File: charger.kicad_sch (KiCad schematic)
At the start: 19 parts, among them U1 IP2326

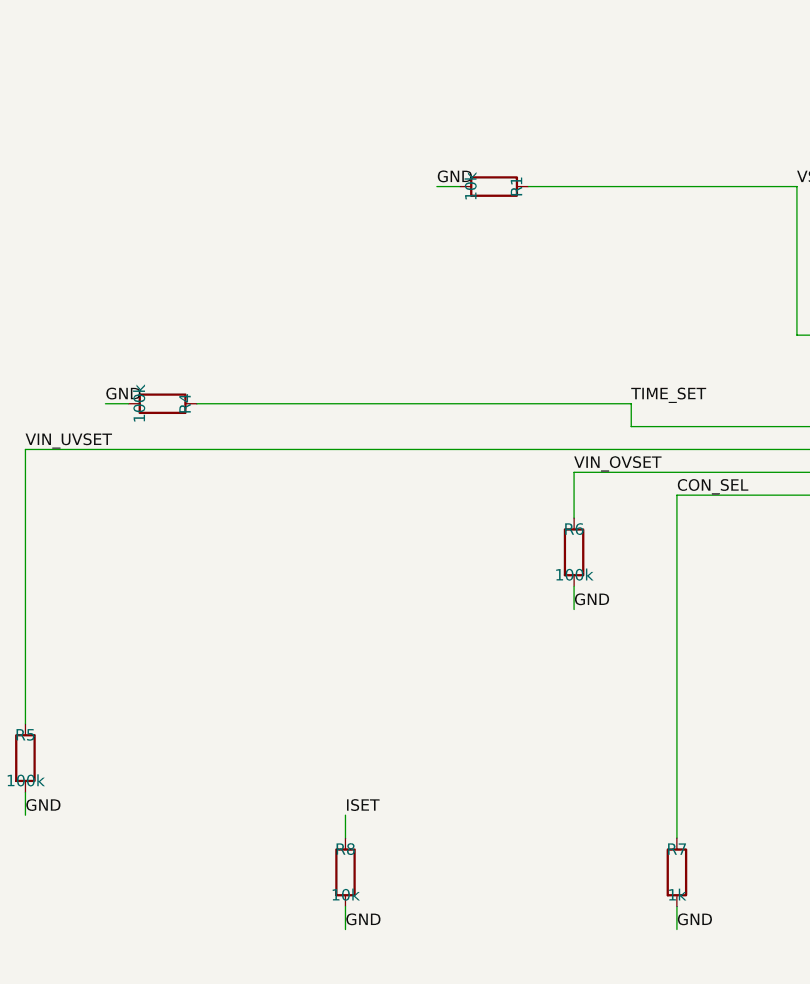
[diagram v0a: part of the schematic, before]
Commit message: components: lock buckboost FETs, R5 SLOPE, and charger config-R values
Buckboost Q1-Q4:
- AON7544 (LCSC C315567), 30V/30A, 5mOhm@10V, DFN-8 3x3, 183k stock,
  ~$0.12 @ qty 1-49.  Extended tier — per feedback_assembly_tier_cost
  memory, that's fine (the cost cliff is Standard-assembly tier, not
  Extended library type).  At 5A steady x 5mOhm = 25mW per FET
  conduction loss, well under the 23W package limit.
- Symbol + footprint + 3D model imported via easyeda2kicad for C315567,
  same workflow as IP2326.

Buckboost R5 (SLOPE):
- Was 10k placeholder.  Set to 20k per LM5176 §9.3.7 slope-compensation
  calc.  Inductor downslope Sn = (Vin_max=12.6V / L=6.8uH) x
  Rcs=5mOhm = ~9.3 mV/us; required Se >= Sn/2 = 4.6 mV/us to avoid
  sub-harmonic oscillation.  20k is TI-EVM starting point at this
  Fsw/L combo; safe against sub-harmonic and leaves loop-tune headroom.
  Notes property records bench-verification guidance.

Charger config-R updates:
- R1 (VSET) 10k → 100k — IP2326 §10 default for 12.6V float on 3S.
- R8 (ISET) 10k → 33k — I_chg ≈ 66/R_iset (kOhm) → 33k = 2A charge,
  0.67C for a 3Ah 3S pack.  Was 10k which would have set an
  unsafe ~6.6A charge rate.
- R2, R3, R4, R5, R6, R9, R10, R7 already at IP2326-typical values
  (verified via table in commit thread); no change needed.

Full-project ERC: 0 errors, 33 cosmetic warnings.  The 2 leftover
"SOIC-8 footprint not found" warnings from the placeholder Device:
Q_NMOS symbols are gone.

Co-Authored-By: Claude Opus 4.7 <noreply@anthropic.com>
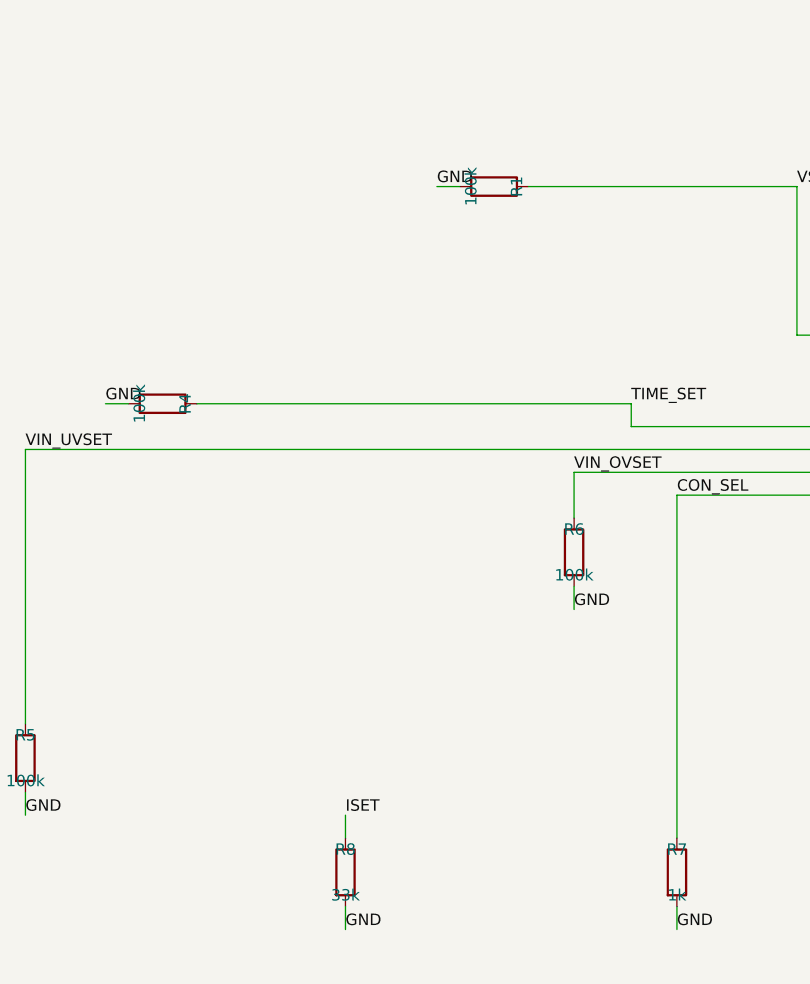
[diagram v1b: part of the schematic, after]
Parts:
- R1: value 10k -> 100k; Notes (none) -> IP2326 VSET default, sets 12.6V float for 3S per datasheet 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
- R8: value 10k -> 33k; Notes (none) -> IP2326 ISET: I_chg ≈ 66 / R_iset (kOhm). 33k → 2A charge = 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

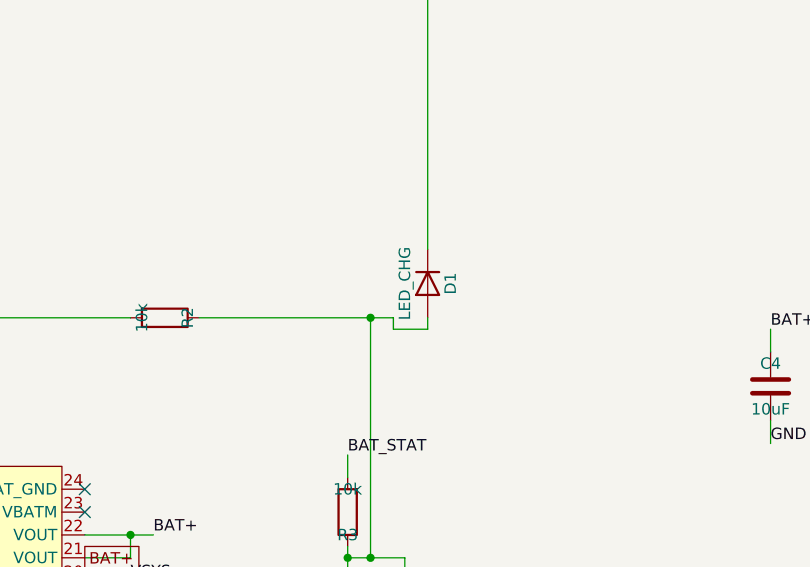
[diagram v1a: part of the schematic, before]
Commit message: sourcing: lock LCSC + MPN + Manufacturer + Footprint for every remaining BOM line
Applied JLCPCB picks (LCSC number + manufacturer part number + tuned
footprint) across all four sub-sheets — 72 components total.  Every
placed component now carries LCSC, MPN, and Manufacturer properties;
the built-in Value/Footprint fields point to the exact JLCPCB stock
unit for that pick.

Highlights:
- ICs (Preferred where available, Extended otherwise):
    U1(bms)      BQ7692003PWR   C601650    TSSOP-20
    U1(charger)  IP2326         C2832094   VQFN-24 EP4x4
    U1(input)    CH224K         C970725    ESSOP-10
    U1(bckbst)   LM5176PWPR     C442493    HTSSOP-28
- Diodes + TVS (all Preferred tier):
    D1(input)    SRV05-4        C7420376   SOT-23-6   (622K stock)
    D2(input)    SMAJ12A        C19077531  SMA        ( 33K stock)
    D1-3(bms)    SMAJ15A        C19077535  SMA        (174K stock)
- Power passives:
    L1(bckbst)   6.8uH 5A       C167221    FXL0630-6R8-M  7x6.6mm
    L1(charger)  2.2uH 4.8A     C602029    FHD4020S-2R2MT 4x4mm
    FB1(input)   600R@100MHz    C139183    CBW160808U601T 0603 (1A)
    R9(bms)      5mR 2W ±1%     C185817    RLM25FEER005   2512
- Bulk passives — Uniohm 0603WAF series, ±1%, high stock.  All caps
  Samsung/Yageo 0603 or 0805 ceramic.  Reused Q1-Q4 = AON7544
  (already locked at 9120877) for bms.Q1/Q2 too — same part
  covers 30V/20A pack-return FET stack.

Effect on pre-fab readiness (kicad-happy):
- SS-001 error CLEARED — 1/34 MPN coverage was blocking pre-fab;
  now 34/34 (100%).
- DS-002 warning shifted: was "no datasheets" (2/34 MPNs), now
  "no datasheets dir" (34/34 MPNs).  Non-blocking; datasheet PDFs
  are nice-to-have but the review can proceed without them.
- 1 remaining error PP-001 (LM5176_VCC no DC source) is a false
  positive: KiCad library symbol declares VCC as power_in but it's
  actually the LM5176's internal 5V LDO OUTPUT.  Accepted as-is.

Full-project ERC still 0 errors.  Schematic is now sourcing-clean
and ready for 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
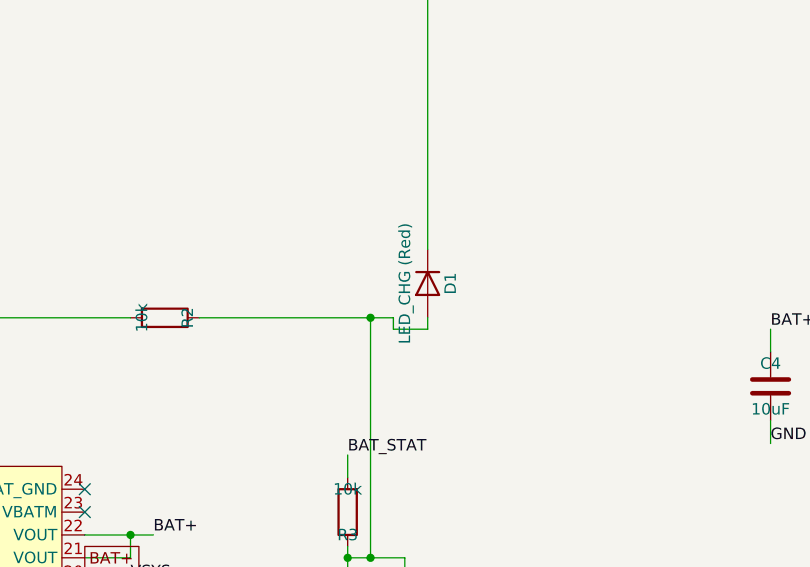
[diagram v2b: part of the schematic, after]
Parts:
- C1, C4: LCSC (none) -> C15850; MPN (none) -> CL21A106KAYNNNE; Manufacturer (none) -> SAMSUNG
- C2, C3: LCSC (none) -> C45783; MPN (none) -> CL21A226MAQNNNE; Manufacturer (none) -> SAMSUNG
- C5: LCSC (none) -> C14663; MPN (none) -> CC0603KRX7R9BB104; Manufacturer (none) -> YAGEO
- D1: value LED_CHG -> LED_CHG (Red); footprint (none) -> LED_SMD:LED_0603_1608Metric; LCSC (none) -> C2286; MPN (none) -> KT-0603R; Manufacturer (none) -> HUBEI KENTO ELEC
- L1: footprint (none) -> Inductor_SMD:L_Sunlord_MWSA0402S; LCSC (none) -> C602029; MPN (none) -> FHD4020S-2R2MT; Manufacturer (none) -> FH (Guangdong Fenghua)
- R1, R4, R5, R6, R9: LCSC (none) -> C25803; MPN (none) -> 0603WAF1003T5E; Manufacturer (none) -> Uniohm
- R10: LCSC (none) -> C23162; MPN (none) -> 0603WAF4701T5E; Manufacturer (none) -> Uniohm
- R2, R3: LCSC (none) -> C25804; MPN (none) -> 0603WAF1002T5E; Manufacturer (none) -> Uniohm
- R7: LCSC (none) -> C21190; MPN (none) -> 0603WAF1001T5E; Manufacturer (none) -> Uniohm
- R8: LCSC (none) -> C4216; MPN (none) -> 0603WAF3302T5E; Manufacturer (none) -> Uniohm
- TH1: footprint (none) -> Resistor_SMD:R_0603_1608Metric; LCSC (none) -> C2889048; MPN (none) -> CMFA 103F3435; Manufacturer (none) -> CHIP-TEK
- U1: footprint (none) -> power_module_lib:VQFN-24_L4.0-W4.0-P0.50-BL-EP2.5; LCSC (none) -> C2832094; MPN (none) -> IP2326; Manufacturer (none) -> INJOINIC

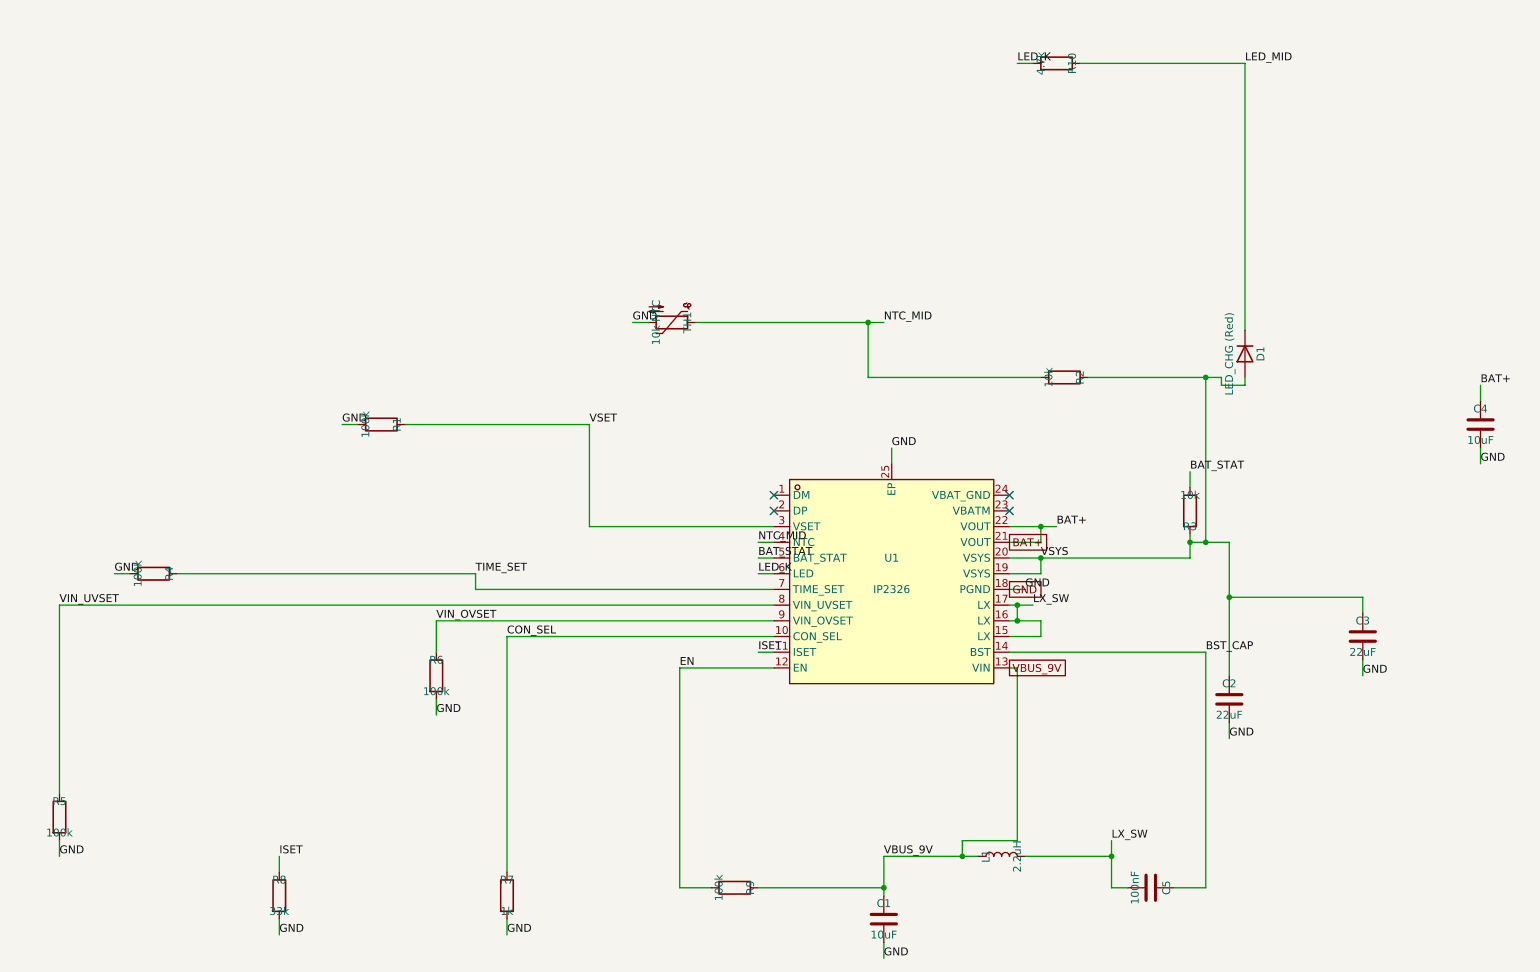
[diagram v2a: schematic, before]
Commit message: sheets: hierarchical ref disambiguation via annotate_schematic
Every sub-sheet symbol now carries a `_{SHEETNAME}{instance_num}` suffix so
refs are globally unique across the hierarchy.  76 refs rewritten:
  bms:       27 (e.g. U1 → U1_BMS1,      Q1 → Q1_BMS1)
  charger:   19 (e.g. U1 → U1_CHARGER1,  R7 → R7_CHARGER1)
  input:      8 (e.g. U1 → U1_INPUT1,    J1 → J1_INPUT1)
  buckboost: 22 (e.g. U1 → U1_BUCKBOOST1,Q1 → Q1_BUCKBOOST1)

Fixes kicad-cli's `schematic has annotation errors` warning which previously
caused BOM export to collapse the four different U1's (BQ76920 + IP2326 +
CH224K + LM5176) into a single row with comma-joined values.

bom_step1.csv committed alongside as the post-disambiguation baseline —
38 grouped rows, 100% LCSC/MPN coverage.

Applied via the new `annotate_schematic` hierarchical pass shipped in
KiCAD-MCP-Server c529efa on develop.  See NOTES.md for the mid-session
handoff block and memory `feedback_hierarchical_annotate`.

Co-Authored-By: Claude Opus 4.7 <noreply@anthropic.com>
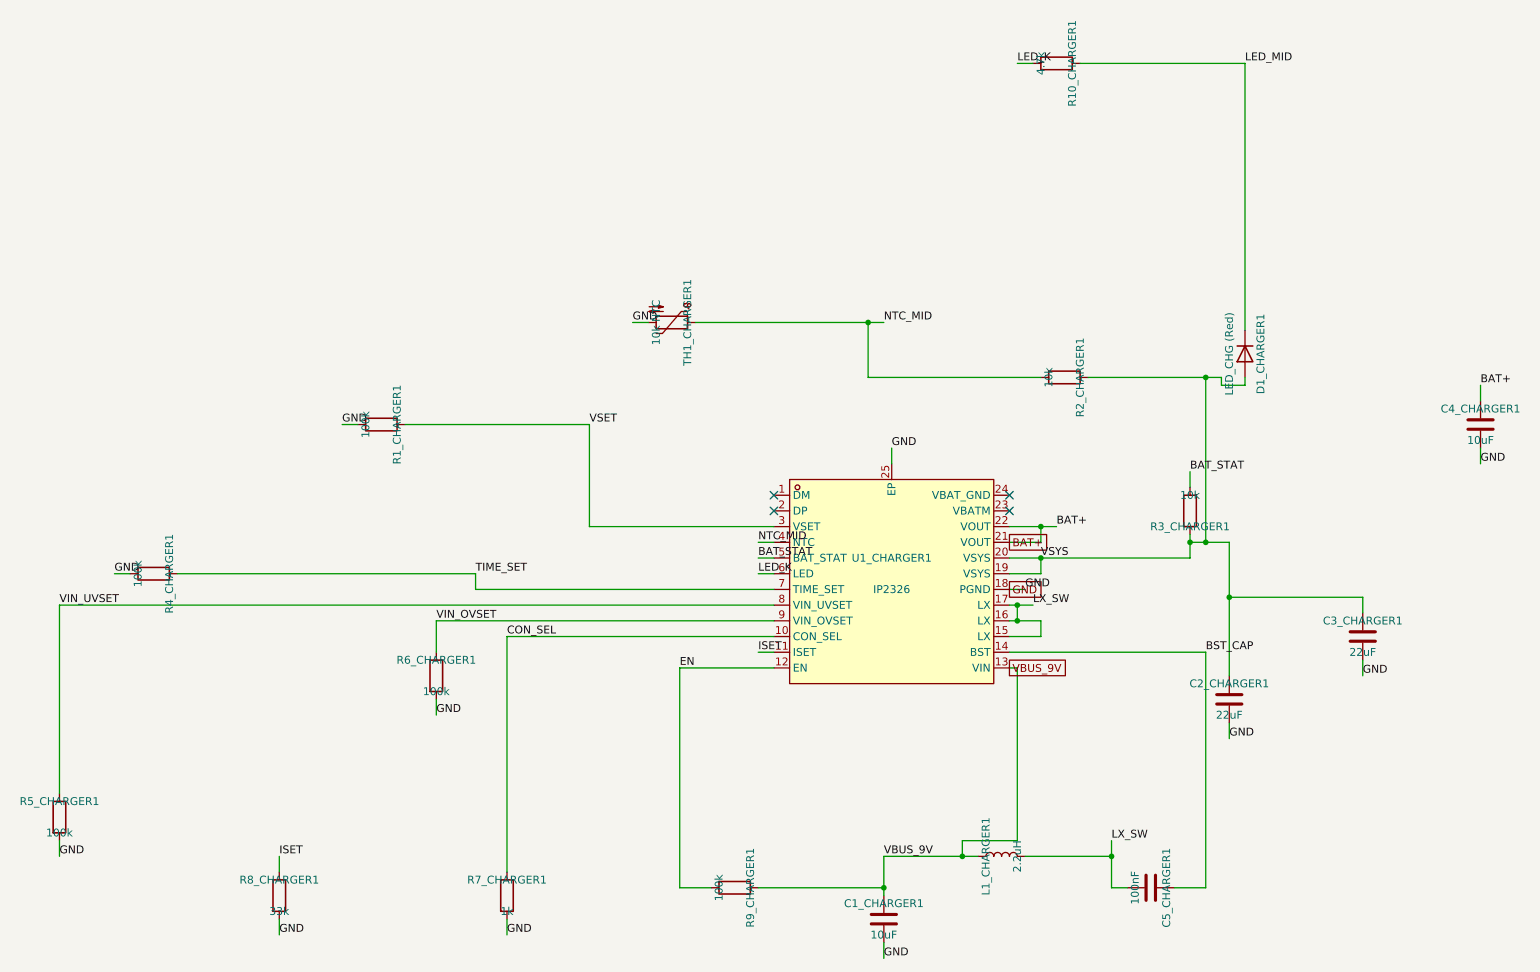
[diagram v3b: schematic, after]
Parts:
- renumbered C1 to C1_CHARGER1, C2 to C2_CHARGER1, C3 to C3_CHARGER1, C4 to C4_CHARGER1, C5 to C5_CHARGER1, D1 to D1_CHARGER1, L1 to L1_CHARGER1, R10 to R10_CHARGER1, R1 to R1_CHARGER1, R2 to R2_CHARGER1, R3 to R3_CHARGER1, R4 to R4_CHARGER1, R5 to R5_CHARGER1, R6 to R6_CHARGER1, R7 to R7_CHARGER1, R8 to R8_CHARGER1, R9 to R9_CHARGER1, TH1 to TH1_CHARGER1, U1 to U1_CHARGER1

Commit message: Step 2: complete Footprint set + sync 76 footprints to .kicad_pcb
Fill in the Footprint properties that were missing from the prior
sourcing pass, and sync everything to the PCB.

Footprint updates on the schematic:
- 35 passives got their Footprint assigned by value (0603 for R/C ≤1uF,
  0805 for 10uF/22uF caps).
- BAT1_BMS1 → power_module_lib:BAT-SMD_BH-18650-B5BA016 (was truncated).
- L1_BUCKBOOST1 → Inductor_SMD:L_Sumida_CDMC6D28_7.25x6.5mm (needed the
  size suffix so KiCad can resolve the .kicad_mod file).

Sync result: 76/76 footprints imported, 60 nets added, 245 pads assigned,
0 import errors.  Unmatched pads reported are all intentional NCs per
REQUIREMENTS.md (USB-C D+/D-, CH224K SBU/CFG, SRV05-4 unused ESD channels).

The footprints are at the default y=-140..-20 auto-import grid; no
placement work yet.  Next step is add_board_outline + set_design_rules.

For discoverability going forward, the pre-sync gap gets caught by
check_sourcing_readiness (KiCAD-MCP-Server fa93ba9 on develop) rather
than having to reset the .kicad_pcb after every retro-fill of an empty
Footprint property.

Co-Authored-By: Claude Opus 4.7 <noreply@anthropic.com>
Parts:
- C1_CHARGER1, C2_CHARGER1, C3_CHARGER1, C4_CHARGER1: footprint (none) -> Capacitor_SMD:C_0805_2012Metric
- C5_CHARGER1: footprint (none) -> Capacitor_SMD:C_0603_1608Metric
- R10_CHARGER1, R1_CHARGER1, R2_CHARGER1, R3_CHARGER1, R4_CHARGER1, R5_CHARGER1, R6_CHARGER1, R7_CHARGER1, R8_CHARGER1, R9_CHARGER1: footprint (none) -> Resistor_SMD:R_0603_1608Metric

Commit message: Step 3+4 WIP: board outline, 4-layer stackup, decoupling spring classes, initial placement pass
Step 3 (board mechanics)
- Edge.Cuts rectangle 100x70 mm (BAT1 alone is 82.3x56.8 so 60x80 in
  the pre-session NOTES was too small)
- 4-layer stackup: added In1.Cu (GND plane) + In2.Cu (PWR plane)
- Design rules tightened: clearance 0.15, minTrackWidth 0.15,
  minViaDiameter 0.45, viaDrill 0.3

Step 4 (WIP — placement)
- 13 Pin_Spring_Class:{pad} = {"IC.pin": "DECOUPLING"} assignments on
  bypass caps across bms/charger/buckboost.  Every IC's power/reservoir/
  bootstrap cap now has an explicit DECOUPLING target so the auto-placer
  parks it right next to the IC pin instead of drifting off with the
  power-rail centroid:
    C7_BMS1        -> BQ76920 CAP1 (pin 7, charge pump reservoir)
    C5_BMS1        -> BQ76920 REGOUT bypass (pin 8)
    C6_BMS1        -> BQ76920 BAT+ sense
    C1..C4_BMS1    -> BQ76920 VCn sense RC filters
    C3_BUCKBOOST1  -> LM5176 BIAS bypass (pin 24, 2.2uF)
    C4_BUCKBOOST1  -> LM5176 VCC LDO bypass (pin 23, 1uF)
    C5_BUCKBOOST1  -> LM5176 BOOT1 bootstrap (pin 26)
    C6_BUCKBOOST1  -> LM5176 BOOT2 bootstrap (pin 20)
    C7_BUCKBOOST1  -> LM5176 SS (pin 8)
    C5_CHARGER1    -> IP2326 BST_CAP (pin 14)
- Initial relax_placement pass with 7 locked anchors (2 headers + BAT1 +
  4 ICs).  Not a shippable layout yet: USB-C is backwards, I2C header
  overlaps BAT1's B.Cu pad zone, Q1..Q4 + L1 (buck-boost power stage)
  scattered from LM5176.  Left as a starting point for hand-refinement.
- TH1_BMS1 (pack thermistor) flipped to B.Cu for proximity to the
  cells — final position to be set by hand.

Co-Authored-By: Claude Opus 4.7 <noreply@anthropic.com>
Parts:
- C5_CHARGER1: Pin_Spring_Class:1 (none) -> {"U1_CHARGER1.14":"DECOUPLING"}
